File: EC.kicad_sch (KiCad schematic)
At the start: 8 parts, among them CN2 B4B-ZR (LF)(SN), CN3 ZH1.5-6P-LT, CN4 B4B-ZR (LF)(SN), J5 Conn_01x10_Socket, J6 Conn_01x10_Socket, U13 B6B-ZR (LF)(SN), U2 B6B-ZR (LF)(SN)

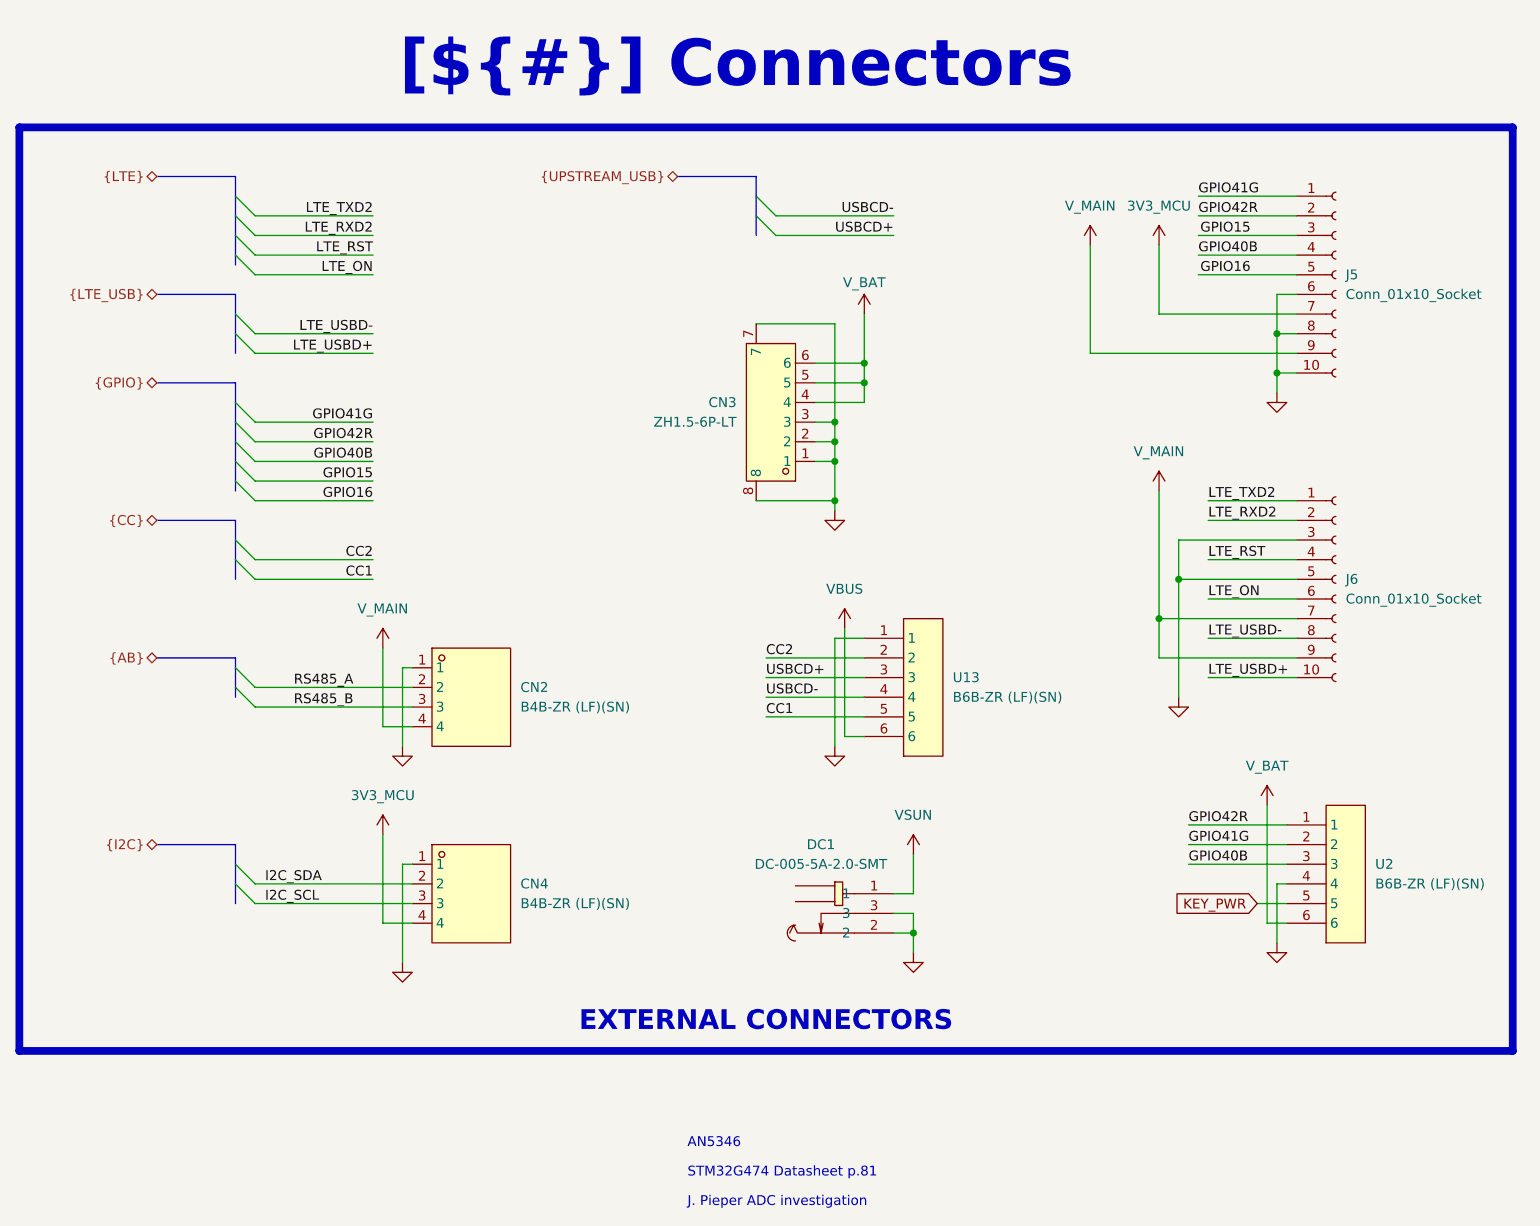
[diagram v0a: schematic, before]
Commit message: [Schematic/PCB][Added] Testpoints test 2
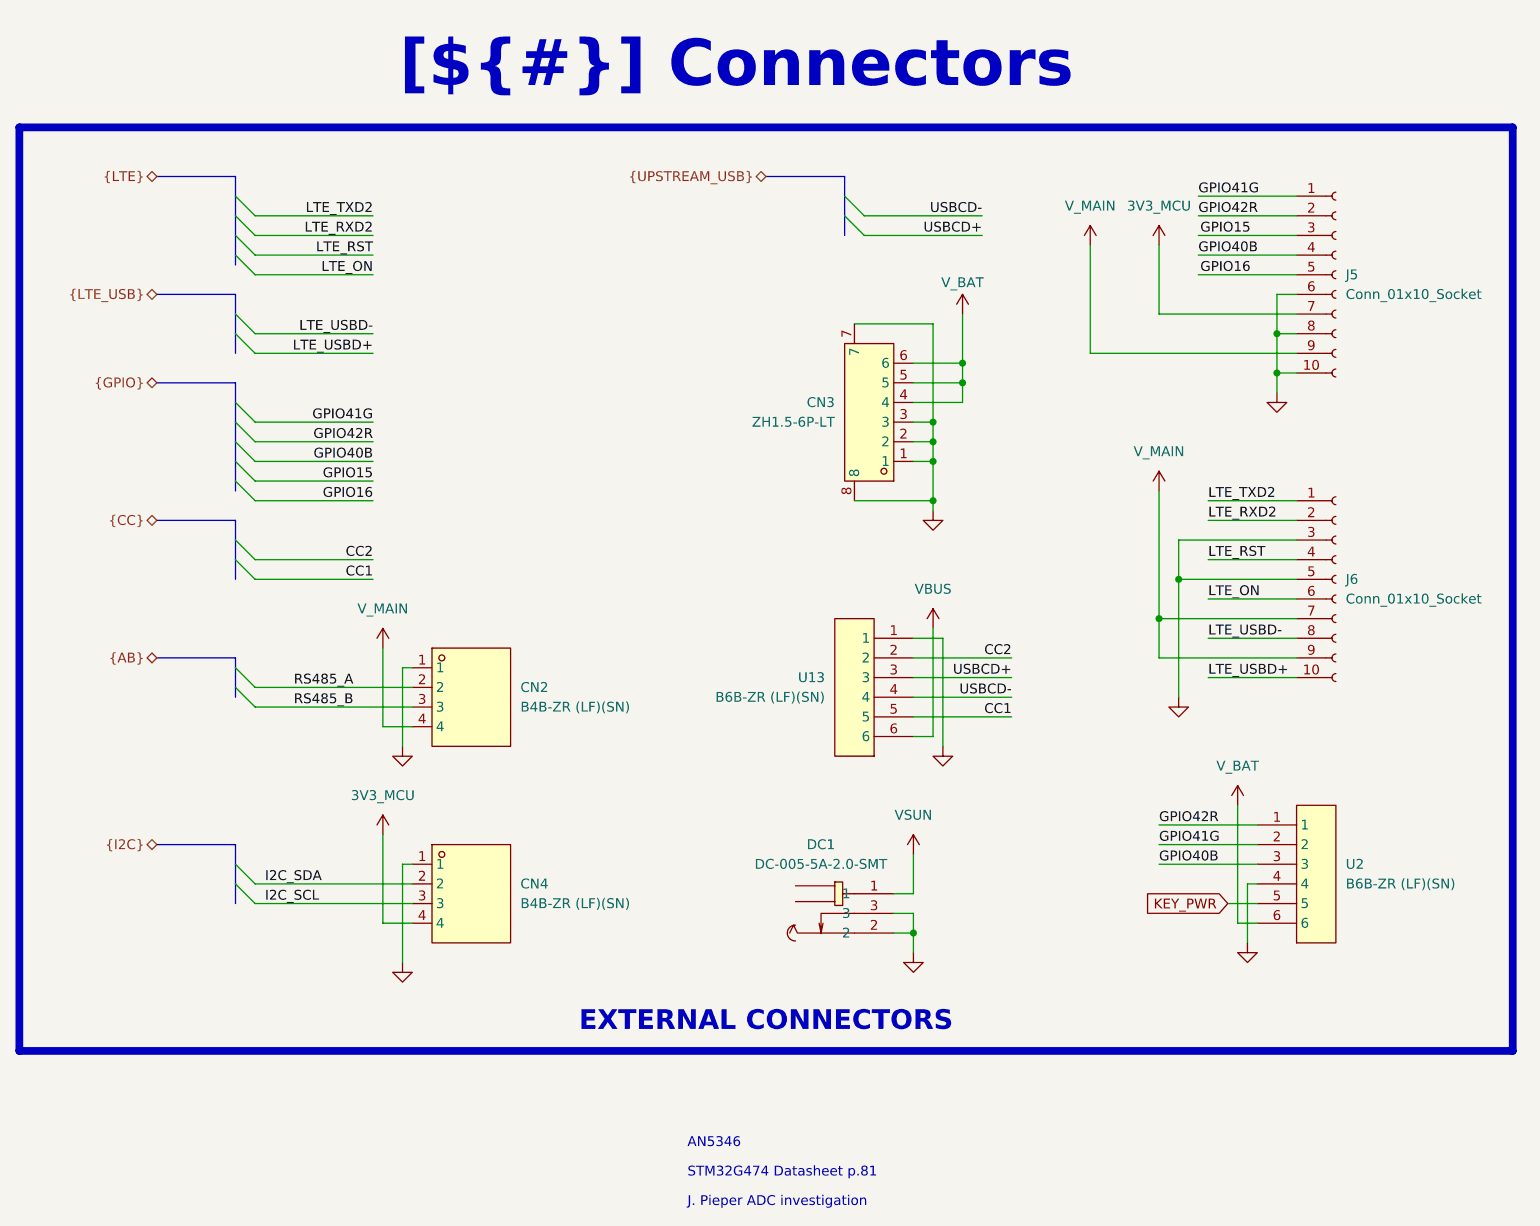
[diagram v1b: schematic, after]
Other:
- moved on the sheet: CN3, U13, U2
